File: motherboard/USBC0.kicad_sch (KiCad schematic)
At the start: 34 parts, among them J5 USB_C_Receptacle, U1 TPD4EUSB30, U2 TPD4EUSB30, U3 TPD4EUSB30, U4 FUSB302BMPX, U5 SY6280AAC

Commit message: work preparing for routing
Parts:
- added J9: Inner USB-C, USB-C:USB-C-SMD_TYPE-C-24P-QT, symbol Connector:USB_C_Receptacle
- added R122: 1M, Resistor_SMD:R_0402_1005Metric, symbol Device:R_Small
- J5: value USB_C_Receptacle -> Outer USB-C
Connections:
- net CC1: now also J9.A5 (CC1)
- net CC2: now also J9.B5 (CC2)
- net GND: now also J9.A1 (GND), J9.A12 (GND), J9.B1 (GND), J9.B12 (GND), R122.2
- net SBUS1: now also J9.A8 (SBU1)
- net SBUS2: now also J9.B8 (SBU2)
- net VBUS: now also J9.A4 (VBUS), J9.A9 (VBUS), J9.B4 (VBUS), J9.B9 (VBUS)
- net IN_TX2+: now reaches C7.1, J5.B2 (TX2+)
- net IN_TX2+: now also J9.B2 (TX2+)
- net IN_RX2+: now reaches J5.A11 (RX2+), R5.1
- net IN_RX2+: now also J9.A11 (RX2+)
- net IN_TX1-: now reaches C4.1, J5.A3 (TX1-)
- net IN_TX1-: now also J9.A3 (TX1-)
- net IN_RX1+: now reaches J5.B11 (RX1+), R7.1
- net IN_RX1+: now also J9.B11 (RX1+)
- net IN_RX2-: now reaches J5.A10 (RX2-), R4.1
- net IN_RX2-: now also J9.A10 (RX2-)
- net IN_RX1-: now reaches J5.B10 (RX1-), R6.1
- net IN_RX1-: now also J9.B10 (RX1-)
- net IN_TX2-: now reaches C6.1, J5.B3 (TX2-)
- net IN_TX2-: now also J9.B3 (TX2-)
- net IN_TX1+: now reaches C5.1, J5.A2 (TX1+)
- net IN_TX1+: now also J9.A2 (TX1+)
- net IN_D+: now reaches CMC1.2, J5.A6 (D+), J5.B6 (D+)
- net IN_D+: now also J9.A6 (D+), J9.B6 (D+)
- net IN_D-: now reaches CMC1.1, J5.A7 (D-), J5.B7 (D-)
- net IN_D-: now also J9.A7 (D-), J9.B7 (D-)
- new net: J9.S1 (SHIELD), R122.1
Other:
- moved on the sheet: J5

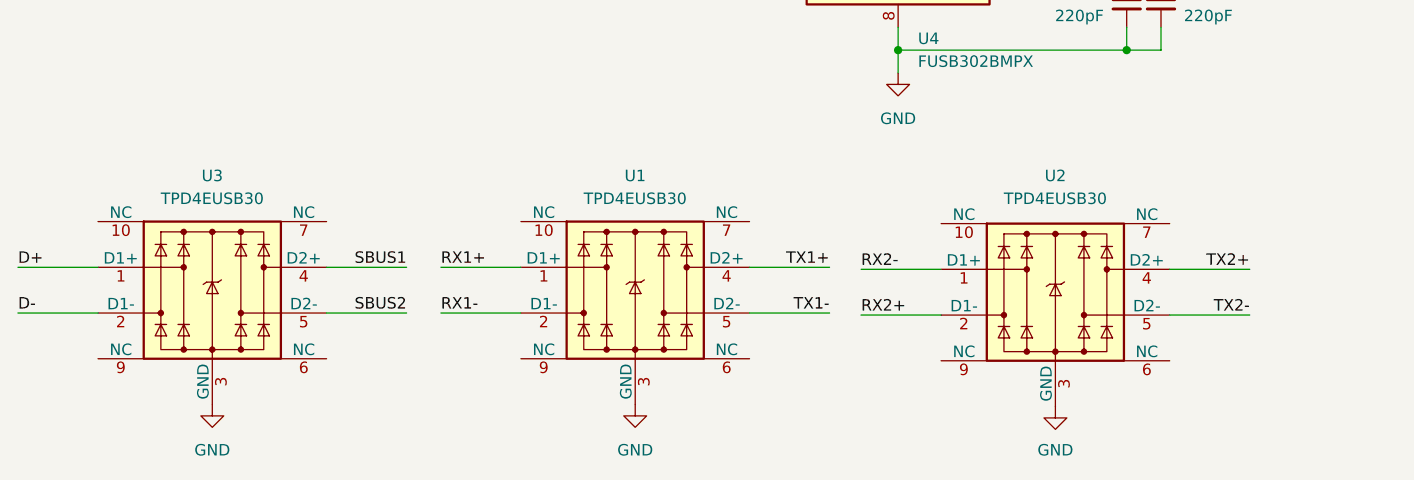
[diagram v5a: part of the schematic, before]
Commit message: component placement of I/O
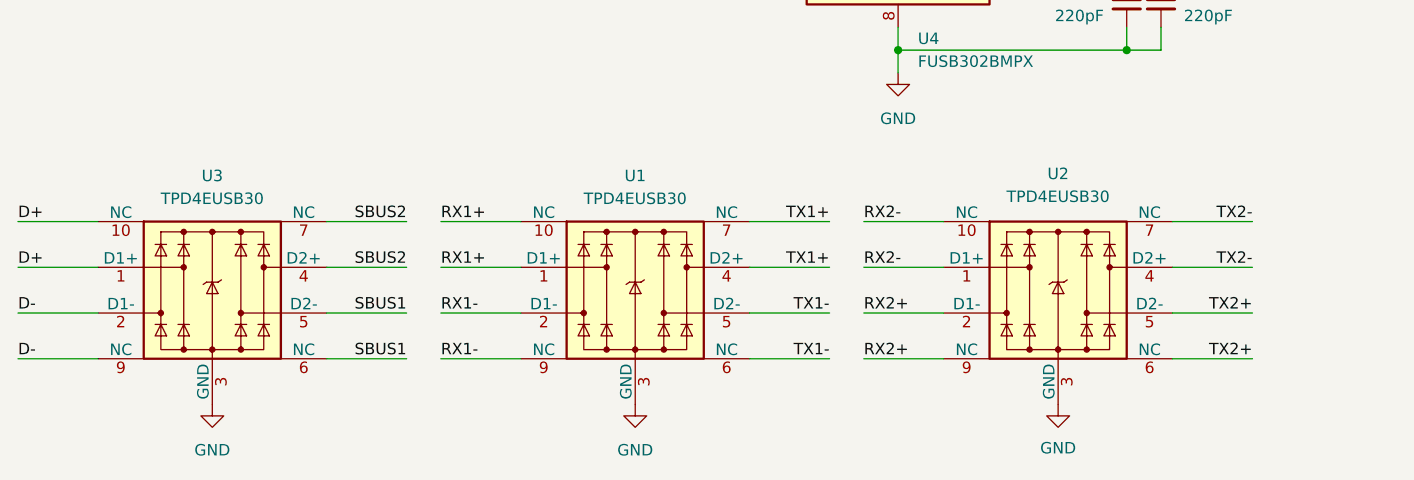
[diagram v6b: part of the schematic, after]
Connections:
- net D+: now also U3.10 (NC)
- net D-: now also U3.9 (NC)
- net IN_D+: now also CMC1.1; no longer CMC1.2
- net IN_D-: now also CMC1.2; no longer CMC1.1
- net RX1+: now also U1.10 (NC)
- net RX1-: now also U1.9 (NC)
- net RX2+: now also U2.9 (NC)
- net RX2-: now also U2.10 (NC)
- net SBUS1: now also U3.5 (D2-), U3.6 (NC); no longer U3.4 (D2+)
- net SBUS2: now also U3.4 (D2+), U3.7 (NC); no longer U3.5 (D2-)
- net TX1+: now also U1.7 (NC)
- net TX1-: now also U1.6 (NC)
- net TX2+: now also U2.5 (D2-), U2.6 (NC); no longer U2.4 (D2+)
- net TX2-: now also U2.4 (D2+), U2.7 (NC); no longer U2.5 (D2-)
- net at R8.1: now also CMC1.3; no longer CMC1.4
- net at R9.1: now also CMC1.4; no longer CMC1.3

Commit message: placement roughly halfway done
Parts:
- removed C4, C5, C6, C7: 100nF, Capacitor_SMD:C_0402_1005Metric, symbol Device:C_Small
- removed D1: LESD8D5.0CB1T5G, Diode_SMD:D_SOD-882, symbol Device:D_TVS_Small_Filled
- removed R4, R5, R6, R7: 0R, Resistor_SMD:R_0402_1005Metric, symbol Device:R_Small
- removed R8, R9: 2.2R, Resistor_SMD:R_0603_1608Metric, symbol Device:R_Small
- added U15: TVS2200DRV, Package_SON:WSON-6-1EP_2x2mm_P0.65mm_EP1x1.6mm, symbol Power_Protection:TVS2200DRV
- C1: value 100nF -> 100nF (+25V)
- C10, C9: value 10uF -> 10uF (C913517); footprint Capacitor_SMD:C_0402_1005Metric -> Capacitor_SMD:C_0603_1608Metric
- U1, U2, U3: value TPD4EUSB30 -> TPD4E02B04
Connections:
- net IN_RX1+ is gone; now on net RX1+: J5.B11 (RX1+), J9.B11 (RX1+)
- net IN_RX1- is gone; now on net RX1-: J5.B10 (RX1-), J9.B10 (RX1-)
- net IN_RX2+ is gone; now on net RX2+: J5.A11 (RX2+), J9.A11 (RX2+)
- net IN_RX2- is gone; now on net RX2-: J5.A10 (RX2-), J9.A10 (RX2-)
- net IN_TX1+ is gone; now on net TX1+: J5.A2 (TX1+), J9.A2 (TX1+)
- net IN_TX1- is gone; now on net TX1-: J5.A3 (TX1-), J9.A3 (TX1-)
- net IN_TX2+ is gone; now on net TX2+: J5.B2 (TX2+), J9.B2 (TX2+)
- net IN_TX2- is gone; now on net TX2-: J5.B3 (TX2-), J9.B3 (TX2-)
- net D+: now also CMC1.4, U3.2 (D1-), U3.9 (NC); no longer U3.1 (D1+), U3.10 (NC)
- net D-: now also CMC1.3, U3.4 (D2+), U3.7 (NC); no longer U3.2 (D1-), U3.9 (NC)
- net GND: now also U15.4 (IN), U15.5 (IN), U15.6 (IN)
- net SBUS2: now also U3.1 (D1+), U3.10 (NC); no longer U3.4 (D2+), U3.7 (NC)
- net VBUS: now also U15.1 (GND), U15.2 (GND), U15.3 (GND), U15.7 (GND)
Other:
- moved on the sheet: C10, CMC1

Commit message: layout nearing completion
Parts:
- C11, C12, C13: footprint Capacitor_SMD:C_0402_1005Metric -> Capacitor_SMD:C_0603_1608Metric
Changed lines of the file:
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@@
 			)
 		)
-		(property "Footprint" "Capacitor_SMD:C_0402_1005Metric"
+		(property "Footprint" "Capacitor_SMD:C_0603_1608Metric"
 			(at 120.65 123.19 0)
 			(effects
@@
 			)
 		)
-		(property "Footprint" "Capacitor_SMD:C_0402_1005Metric"
+		(property "Footprint" "Capacitor_SMD:C_0603_1608Metric"
 			(at 163.83 91.44 0)
 			(effects
@@
 			)
 		)
-		(property "Footprint" "Capacitor_SMD:C_0402_1005Metric"
+		(property "Footprint" "Capacitor_SMD:C_0603_1608Metric"
 			(at 135.89 91.44 0)
 			(effects
